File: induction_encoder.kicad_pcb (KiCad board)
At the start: 4 copper layers, 136 x 136 mm, 72 parts, among them J2 Conn_01x06, U1 MT9105ET, U10 IPS2200, U11 ADS1115IDGS, U12 ADS1115IDGS, U2 MT9105ET, U3 MT9105ET, U4 MT9105ET, U5 MT9105ET, U6 MT9105ET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

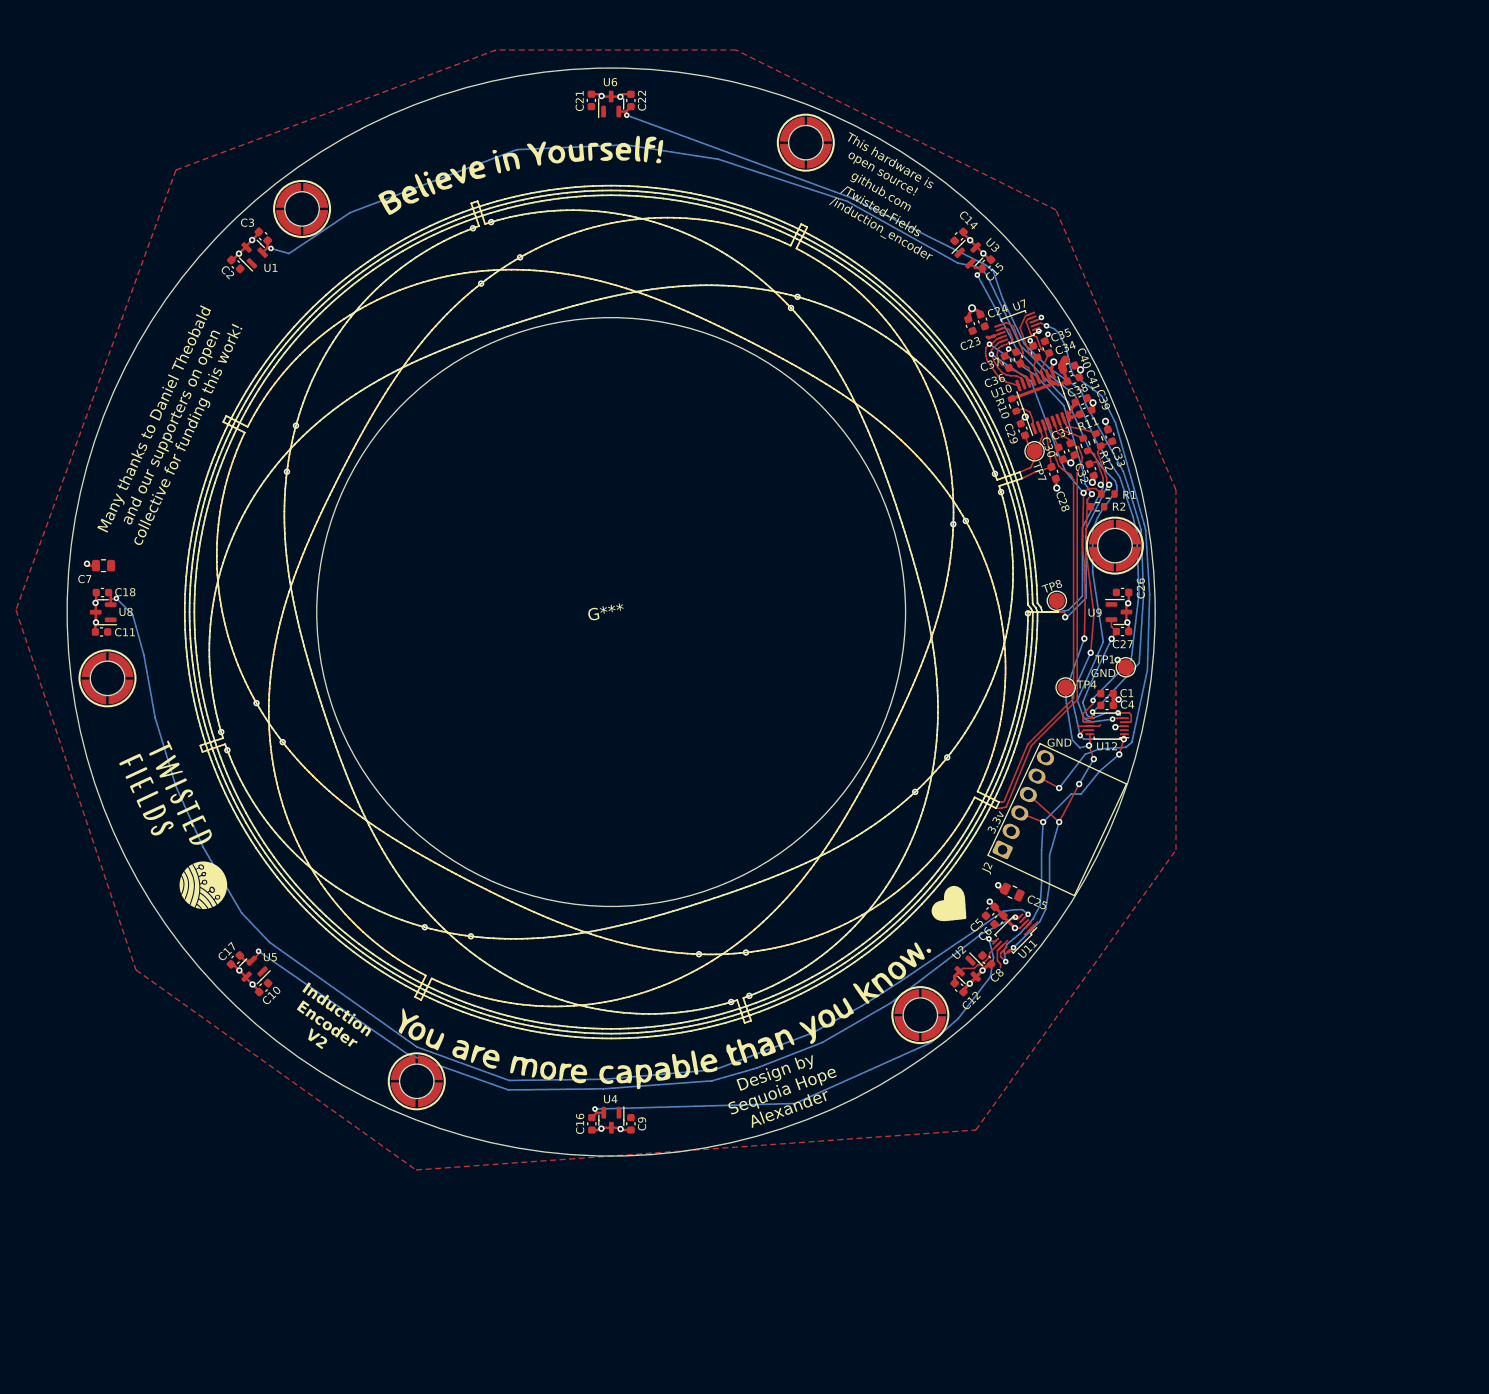
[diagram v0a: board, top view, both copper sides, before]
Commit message: initial layout for 100-170mm induction encoder
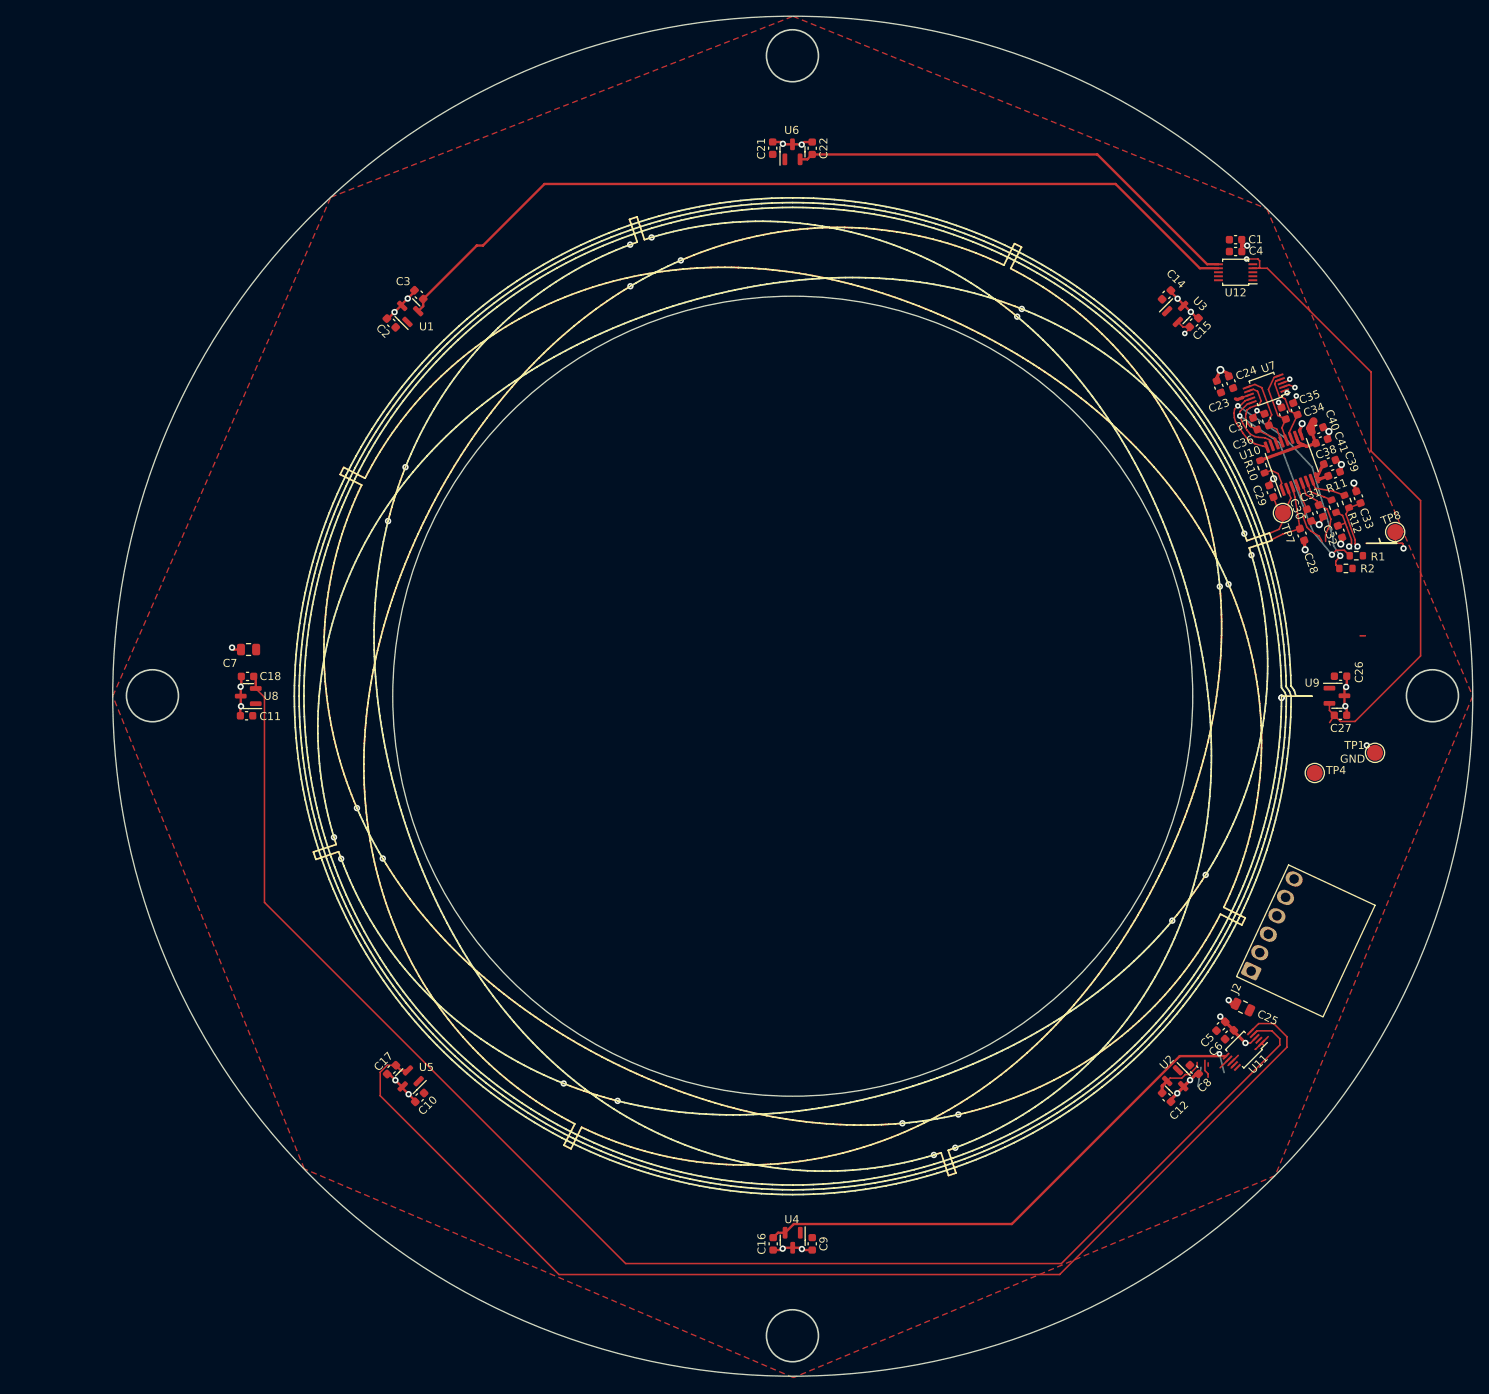
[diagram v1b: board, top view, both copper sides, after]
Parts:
- removed G***: LOGO, taylor_footprints:twisted
- removed G***: LOGO, taylor_footprints:twisted_icon
- removed G***: LOGO, taylor_footprints:twisted_2
- removed G***: LOGO, parts:believe
- removed H1, H2, H3, H4, H5, H6: MountingHole, encoder:SMD_BD5.6-D4.1
- moved C4 59.0 mm to (178.1, 54.9)
- moved U12 59.0 mm to (178.1, 57.5)
- moved C1 59.0 mm to (178.1, 53.5)
- moved JP1 50.3 mm to (193.9, 103.0), turned to 0 degrees
- moved JP2 43.2 mm to (198.4, 91.4)
- moved TP8 43.2 mm to (198.0, 90.0)
- moved J2 34.6 mm to (179.7, 144.7)
- moved TP1 32.9 mm to (195.5, 117.6)
- moved TP4 32.9 mm to (188.0, 120.1)
- moved C25 32.2 mm to (179.0, 149.4)
- moved C5 32.2 mm to (176.2, 151.8)
- moved C6 32.2 mm to (177.3, 152.8)
- moved U11 32.2 mm to (179.1, 154.7)
- moved C33 32.0 mm to (193.4, 85.7)
- moved R2 32.0 mm to (191.8, 94.5)
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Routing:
- net (no net): track 0.00 -> 1900.4 mm, vias 0 -> 10
- net TX+: track 1025.7 -> 11.8 mm, vias 2 -> 1
- net 1+: track 649.5 -> 8.37 mm, vias 8 -> 0
- net 2: track 616.2 -> 746.1 mm
- net SDA: track 113.8 -> 36.2 mm, vias 8 -> 2
- net RDY: track 72.5 -> 1.57 mm, vias 2 -> 1
- net SCL: track 102.6 -> 32.8 mm, vias 8 -> 2
- net /MAG2: track 70.8 -> 2.81 mm, vias 2 -> 1
- net /MAG3: track 116.4 -> 58.2 mm, vias 2 -> 0
- net /MAG1: track 20.8 -> 78.2 mm, vias 2 -> 1
- net /MAG4: track 163.5 -> 111.5 mm, vias 2 -> 0
- net 1-: track 53.6 -> 9.10 mm
- net /MAG6: track 108.8 -> 148.4 mm, vias 2 -> 0
- net /MAG5: track 156.6 -> 190.5 mm, vias 2 -> 0
- net TX-: track 26.2 -> 8.13 mm
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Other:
- board size 136 x 136 mm -> 170 x 170 mm
- board text removed: "/Twisted-Fields"
- board text removed: "/induction_encoder"
- board text removed: "3.3v"
- board text removed: "Design by Sequoia Hope Alexander"
- board text removed: "Induction Encoder V2"
- board text removed: "Many thanks to Daniel Theobald and our supporters on open collective for funding this work!"
- board text removed: "This hardware is open source!"
- board text removed: "github.com"

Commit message: layout finished for 100-170mm induction encoder
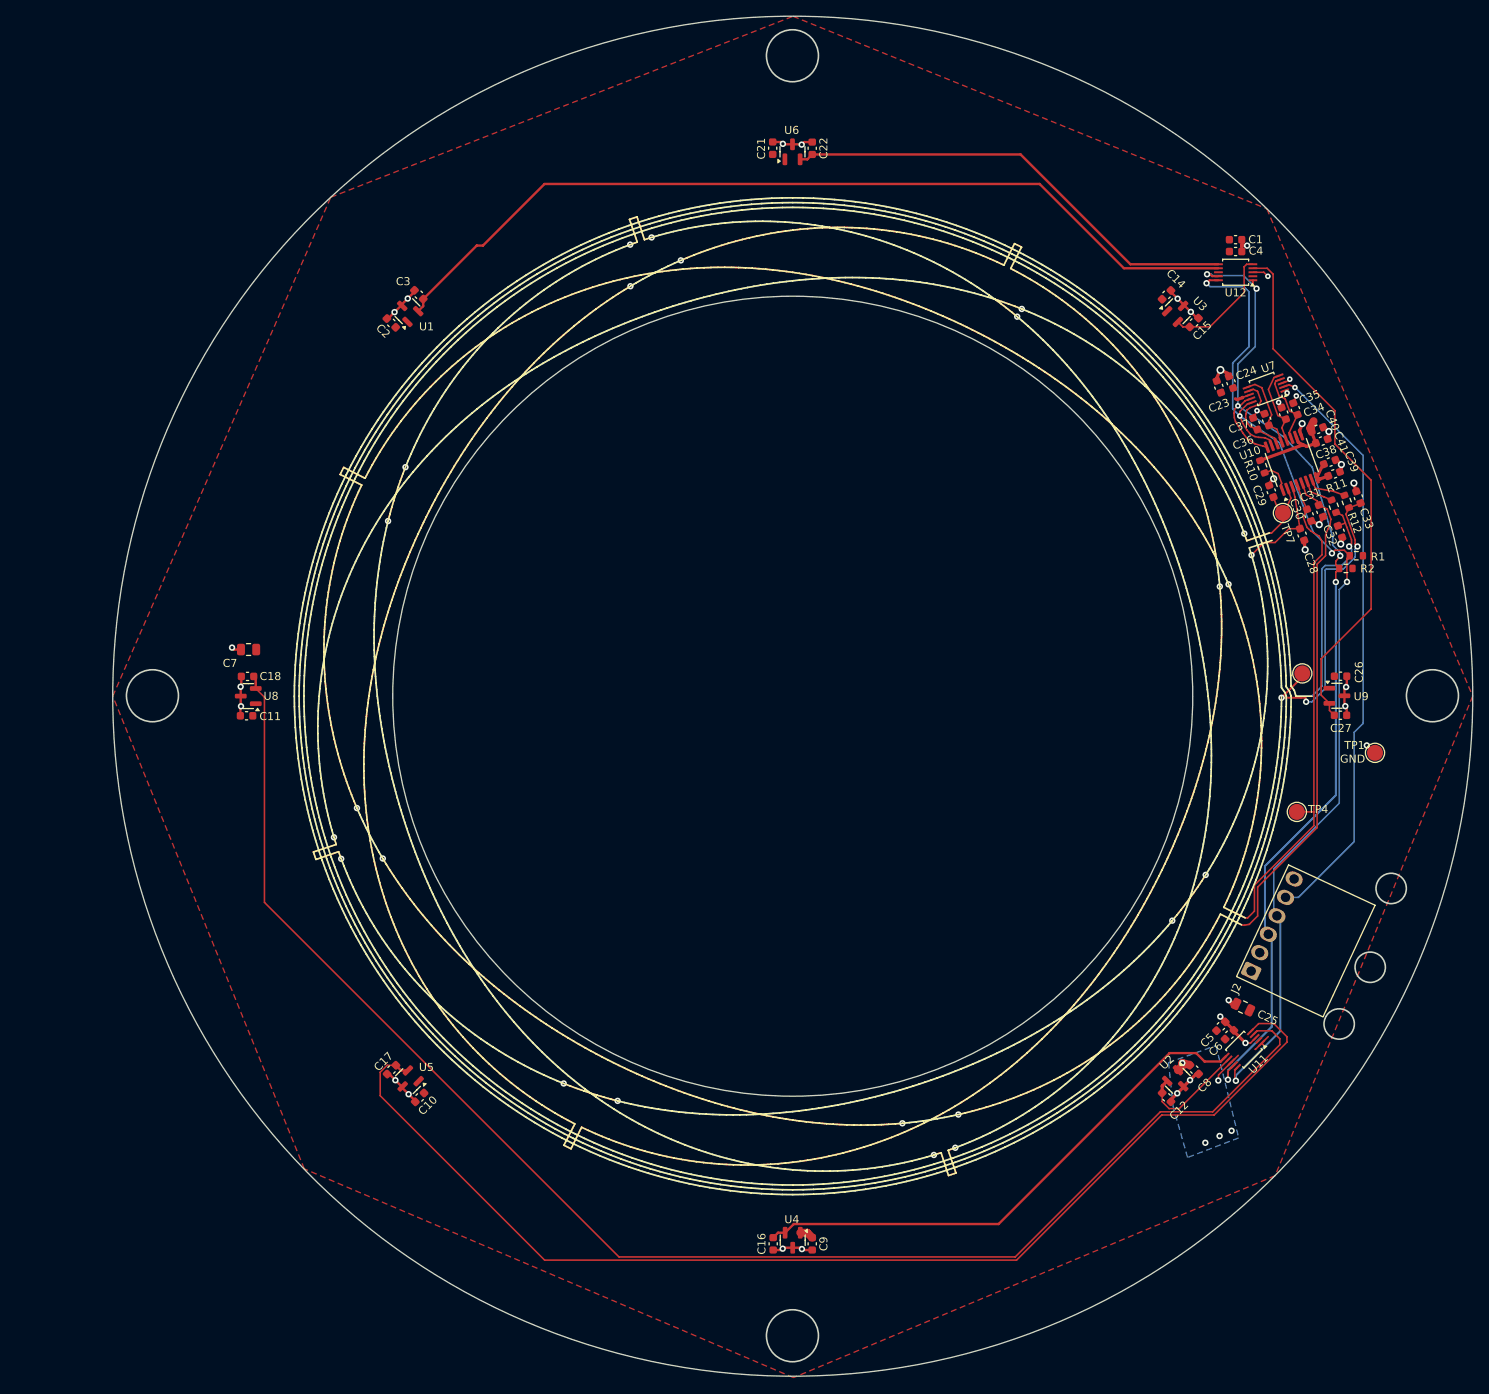
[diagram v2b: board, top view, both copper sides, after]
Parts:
- R10: value 10k -> 10K
- moved JP1 38.9 mm to (179.5, 139.1), turned to -170 degrees
- moved JP2 22.7 mm to (186.5, 110.7)
- moved TP8 21.1 mm to (186.4, 107.7)
- moved TP4 5.35 mm to (185.7, 125.0)
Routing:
- net (no net): track 1900.4 -> 0.00 mm, vias 10 -> 0
- net TX+: track 11.8 -> 1199.6 mm, vias 1 -> 2
- net 1+: track 8.37 -> 788.4 mm, vias 0 -> 8
- net SCL: track 32.8 -> 131.7 mm, vias 2 -> 5
- net SDA: track 36.2 -> 133.8 mm, vias 2 -> 6
- net RDY: track 1.57 -> 73.8 mm
- net 1-: track 9.10 -> 60.9 mm
- net TX-: track 8.13 -> 31.3 mm
- net /MAG2: track 2.81 -> 15.0 mm, vias 1 -> 0
- net /MAG1: track 78.2 -> 66.5 mm, vias 1 -> 0
- net /MAG8: track 8.29 -> 14.1 mm
- net /MAG7: track 71.8 -> 66.9 mm, vias 1 -> 0
- net +3V3: track 20.6 -> 25.3 mm, vias 0 -> 5
- net GND: track 76.6 -> 78.6 mm, vias 36 -> 37
- net /MAG6: track 148.4 -> 146.5 mm
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- added copper zone on B.Cu, net +3V3
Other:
- outline, holes or cut-outs redrawn

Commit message: 100-170mm version ordered November 2024
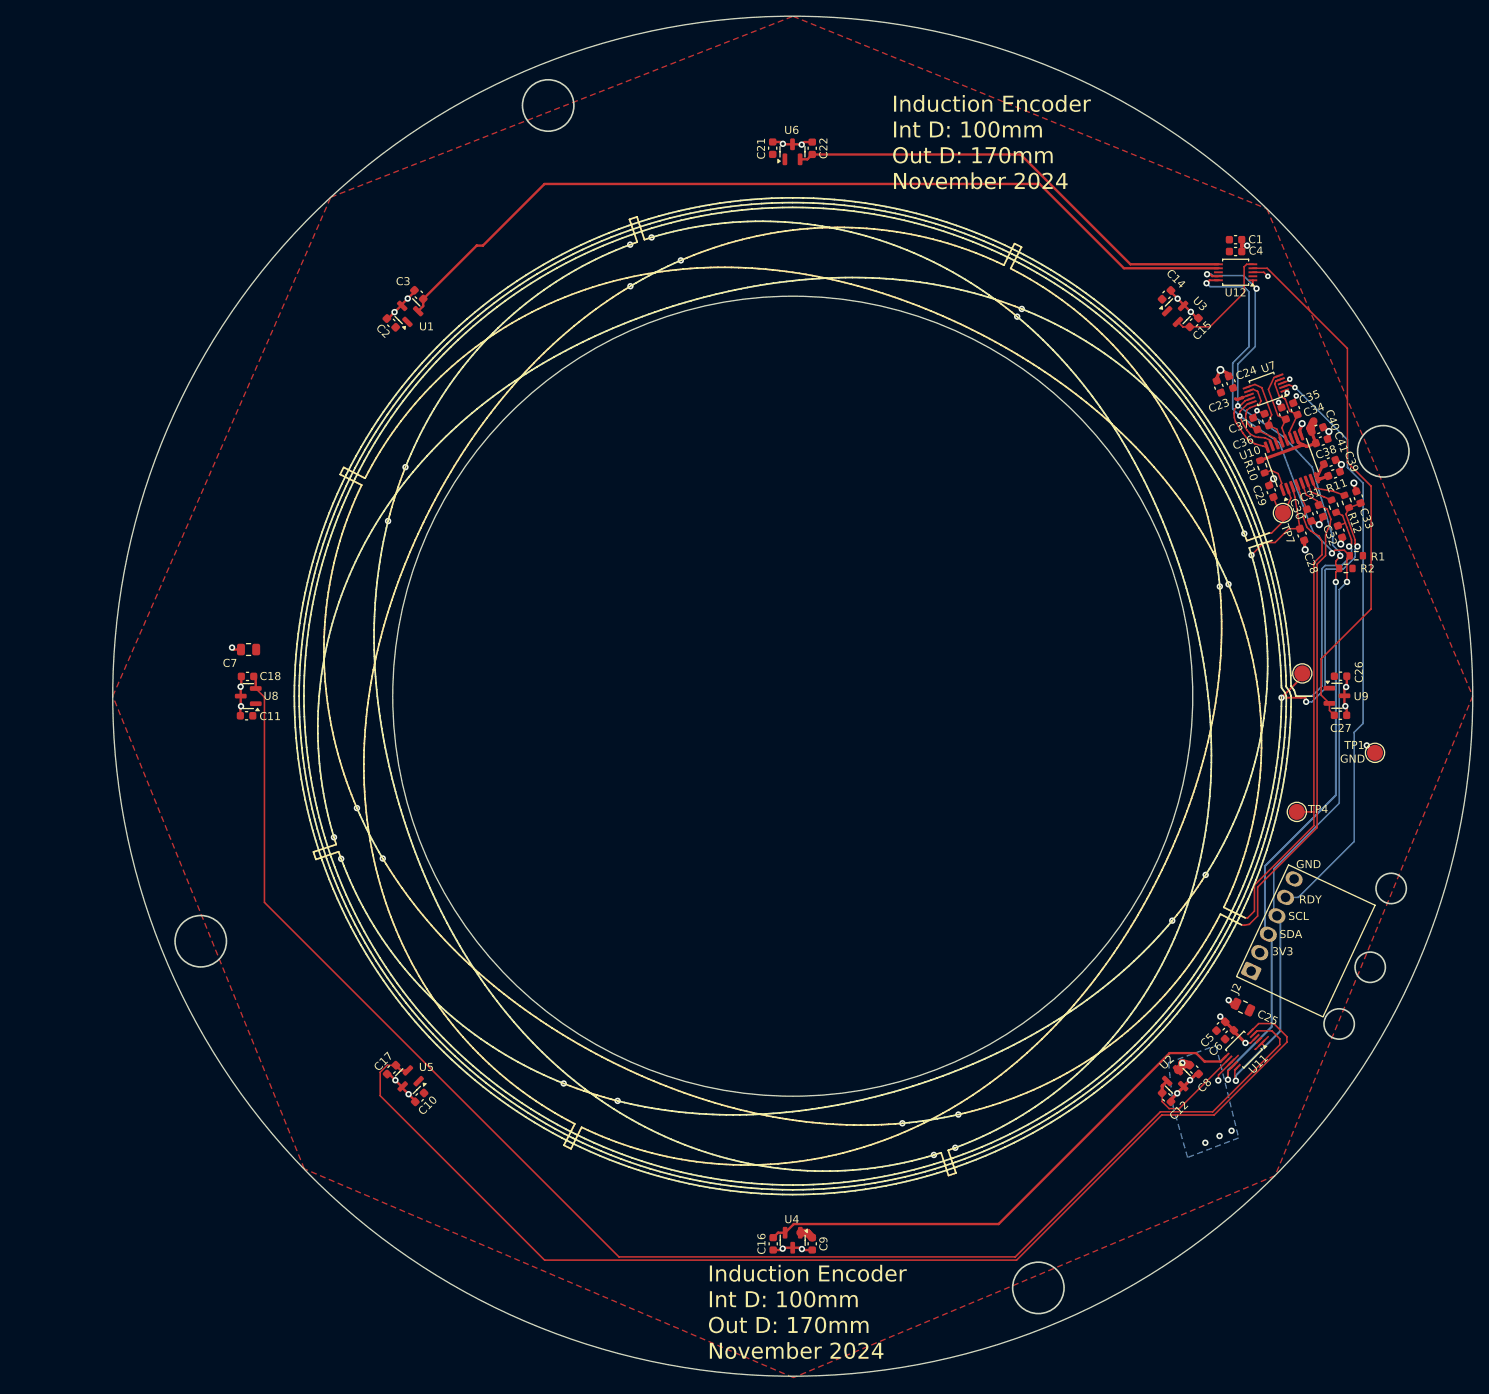
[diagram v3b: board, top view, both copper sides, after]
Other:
- outline, holes or cut-outs redrawn
- board text added: "3V3"
- board text added: "Induction Encoder Int D: 100mm Out D: 170mm November 2024"
- board text added: "RDY"
- board text added: "SCL"
- board text added: "SDA"
